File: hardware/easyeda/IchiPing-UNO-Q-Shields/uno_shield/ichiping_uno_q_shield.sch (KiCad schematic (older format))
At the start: 12 parts

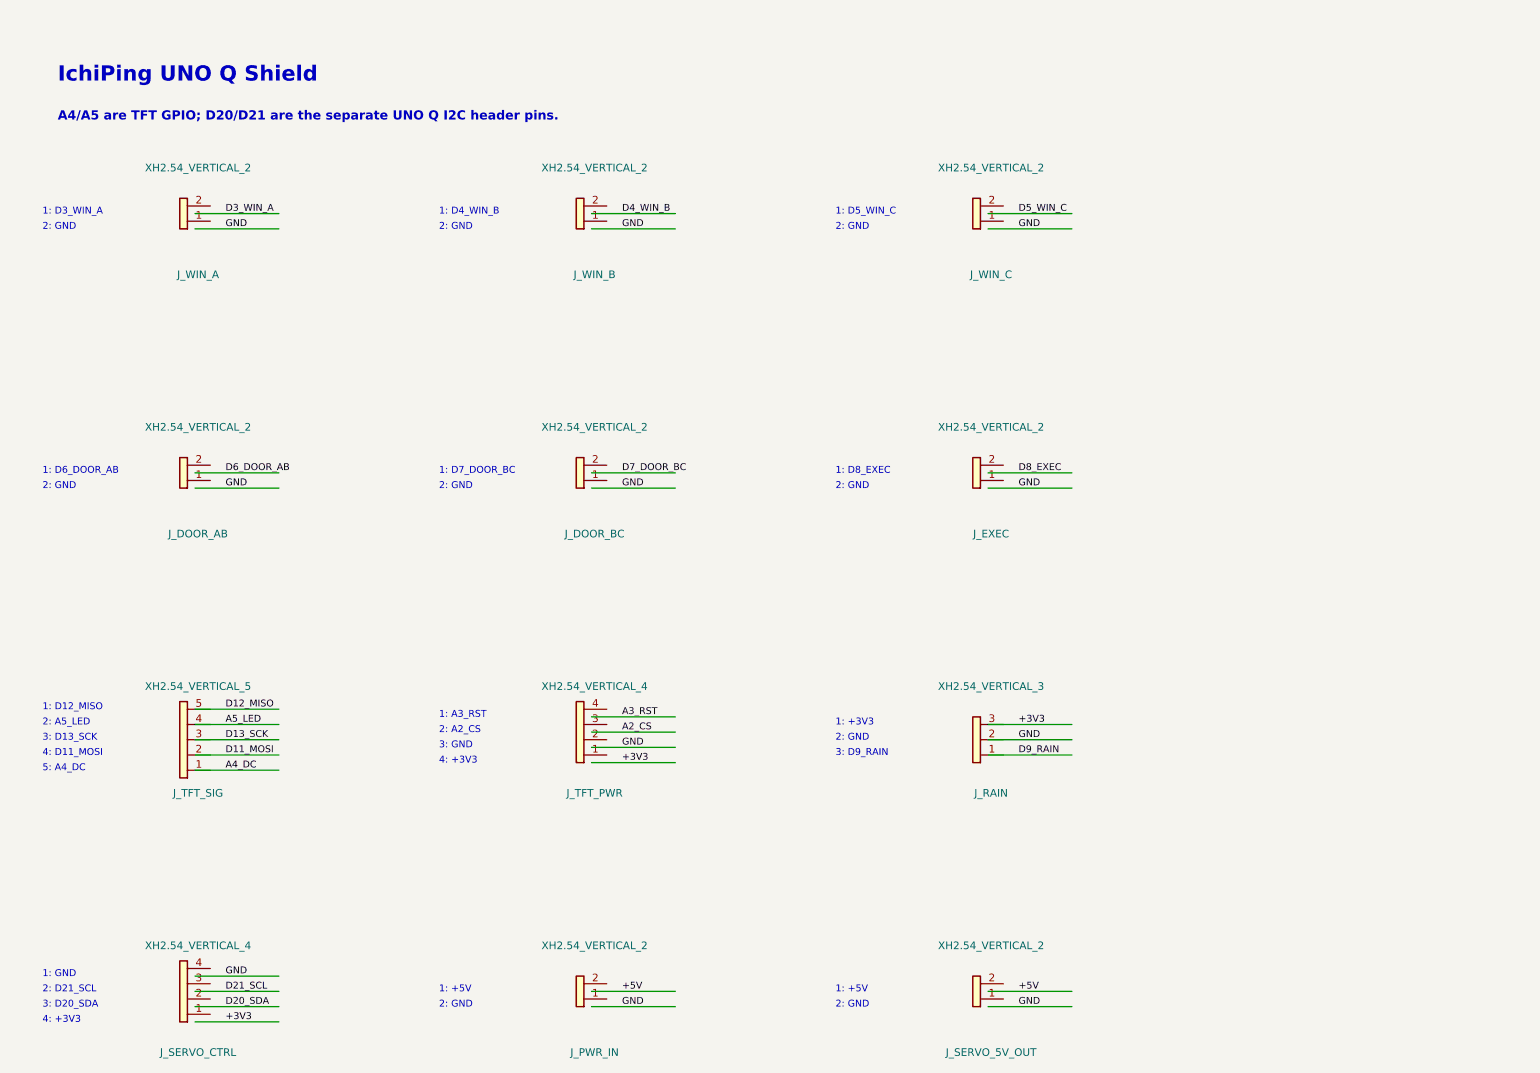
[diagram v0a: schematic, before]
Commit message: Add UNO shield schematic and EasyEDA DRC setup
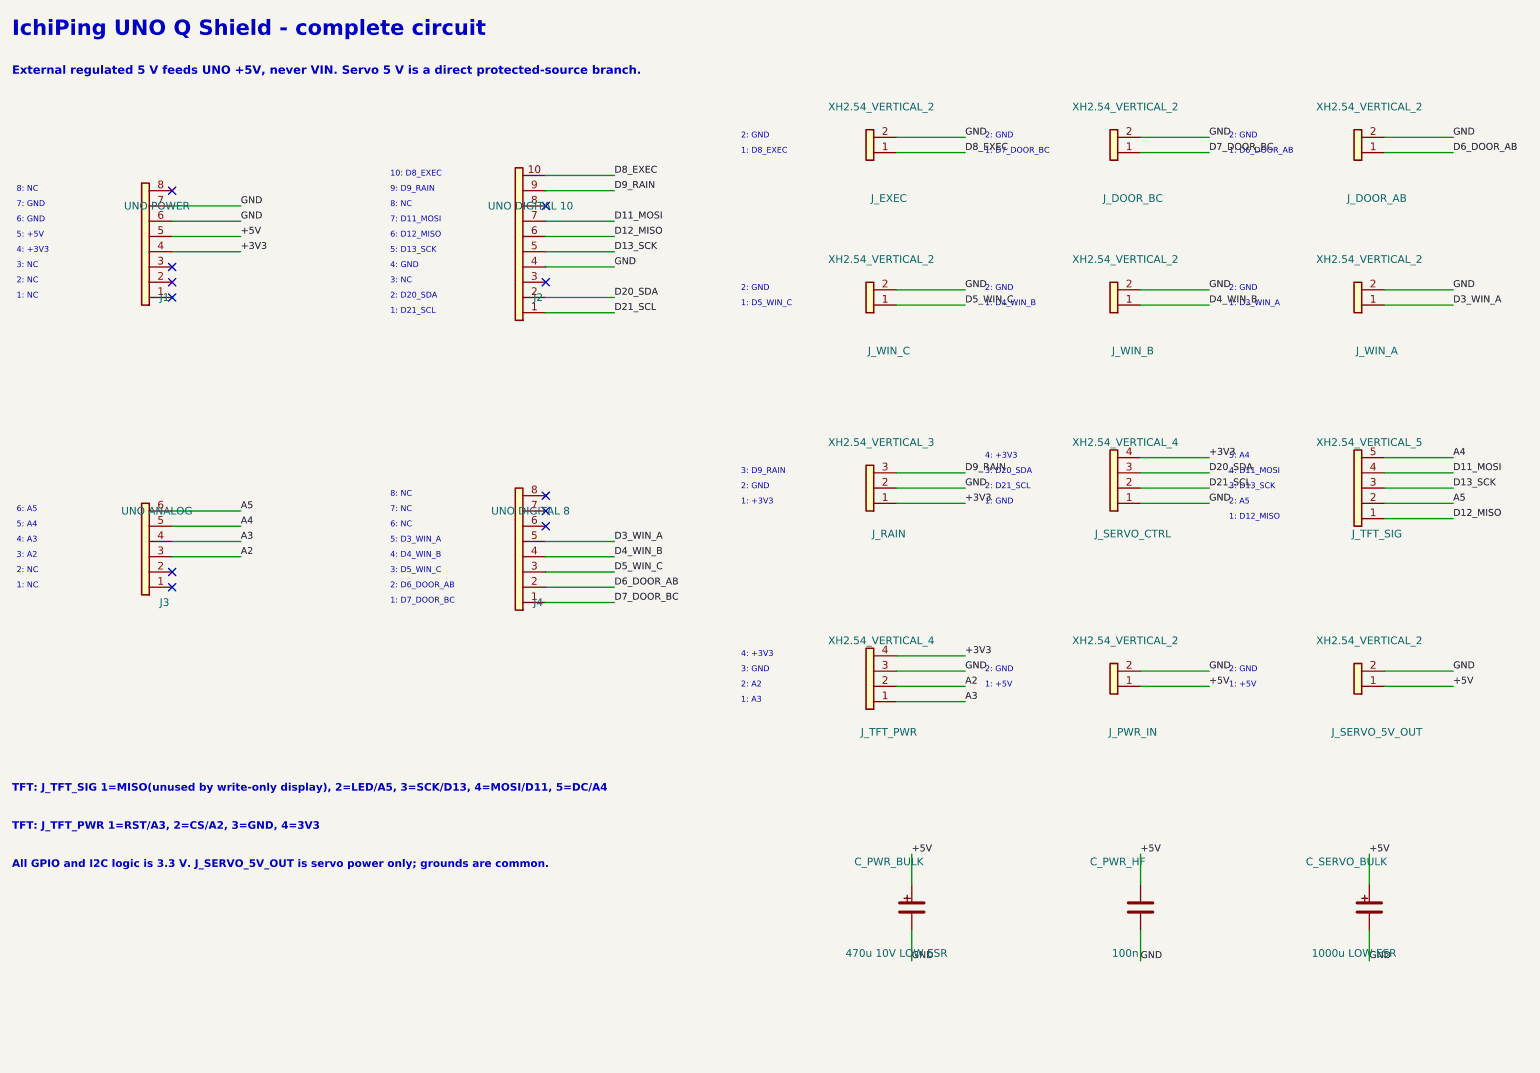
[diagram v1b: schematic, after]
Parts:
- added C_PWR_BULK: 470u 10V LOW ESR, Capacitor_THT:CP_Radial_D8.0mm_P3.50mm, symbol Device:C_Polarized
- added C_PWR_HF: 100n, Capacitor_THT:C_Disc_D5.0mm_W2.5mm_P5.00mm, symbol Device:C
- added C_SERVO_BULK: 1000u LOW ESR, Capacitor_THT:CP_Radial_D10.0mm_P5.00mm, symbol Device:C_Polarized
- added J1: UNO POWER, Connector_PinHeader_2.54mm:PinSocket_1x08_P2.54mm_Vertical, symbol Connector_Generic:Conn_01x08
- added J2: UNO DIGITAL 10, Connector_PinHeader_2.54mm:PinSocket_1x10_P2.54mm_Vertical, symbol Connector_Generic:Conn_01x10
- added J3: UNO ANALOG, Connector_PinHeader_2.54mm:PinSocket_1x06_P2.54mm_Vertical, symbol Connector_Generic:Conn_01x06
- added J4: UNO DIGITAL 8, Connector_PinHeader_2.54mm:PinSocket_1x08_P2.54mm_Vertical, symbol Connector_Generic:Conn_01x08
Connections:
- net labels added: A2, A3, A4, A5
- net labels removed: A2_CS, A3_RST, A4_DC, A5_LED
- wire segments 32 -> 59
- no-connect marks 0 -> 11
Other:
- note added: "10: D8_EXEC"
- note added: "1: A3"
- note added: "1: D21_SCL"
- note added: "1: NC"
- note added: "2: A2"
- note added: "2: A5"
- note added: "2: D20_SDA"
- note added: "2: D6_DOOR_AB"
- note added: "2: NC"
- note added: "3: A2"
- note added: "3: D5_WIN_C"
- note added: "3: NC"
- note added: "4: A3"
- note added: "4: D4_WIN_B"
- note added: "4: GND"
- note added: "5: +5V"
- note added: "5: A4"
- note added: "5: D13_SCK"
- note added: "5: D3_WIN_A"
- note added: "6: A5"
- note added: "6: D12_MISO"
- note added: "6: GND"
- note added: "6: NC"
- note added: "7: D11_MOSI"
- note added: "7: GND"
- note added: "7: NC"
- note added: "8: NC"
- note added: "9: D9_RAIN"
- note added: "All GPIO and I2C logic is 3.3 V. J_SERVO_5V_OUT is servo power only; grounds are common."
- note added: "External regulated 5 V feeds UNO +5V, never VIN. Servo 5 V is a direct protected-source branch."
- note added: "IchiPing UNO Q Shield - complete circuit"
- note added: "TFT: J_TFT_PWR 1=RST/A3, 2=CS/A2, 3=GND, 4=3V3"
- note added: "TFT: J_TFT_SIG 1=MISO(unused by write-only display), 2=LED/A5, 3=SCK/D13, 4=MOSI/D11, 5=DC/A4"
- note removed: "1: A3_RST"
- note removed: "2: A2_CS"
- note removed: "2: A5_LED"
- note removed: "5: A4_DC"
- note removed: "A4/A5 are TFT GPIO; D20/D21 are the separate UNO Q I2C header pins."
- note removed: "IchiPing UNO Q Shield"
